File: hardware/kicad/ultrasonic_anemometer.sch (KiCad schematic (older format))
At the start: 0 parts

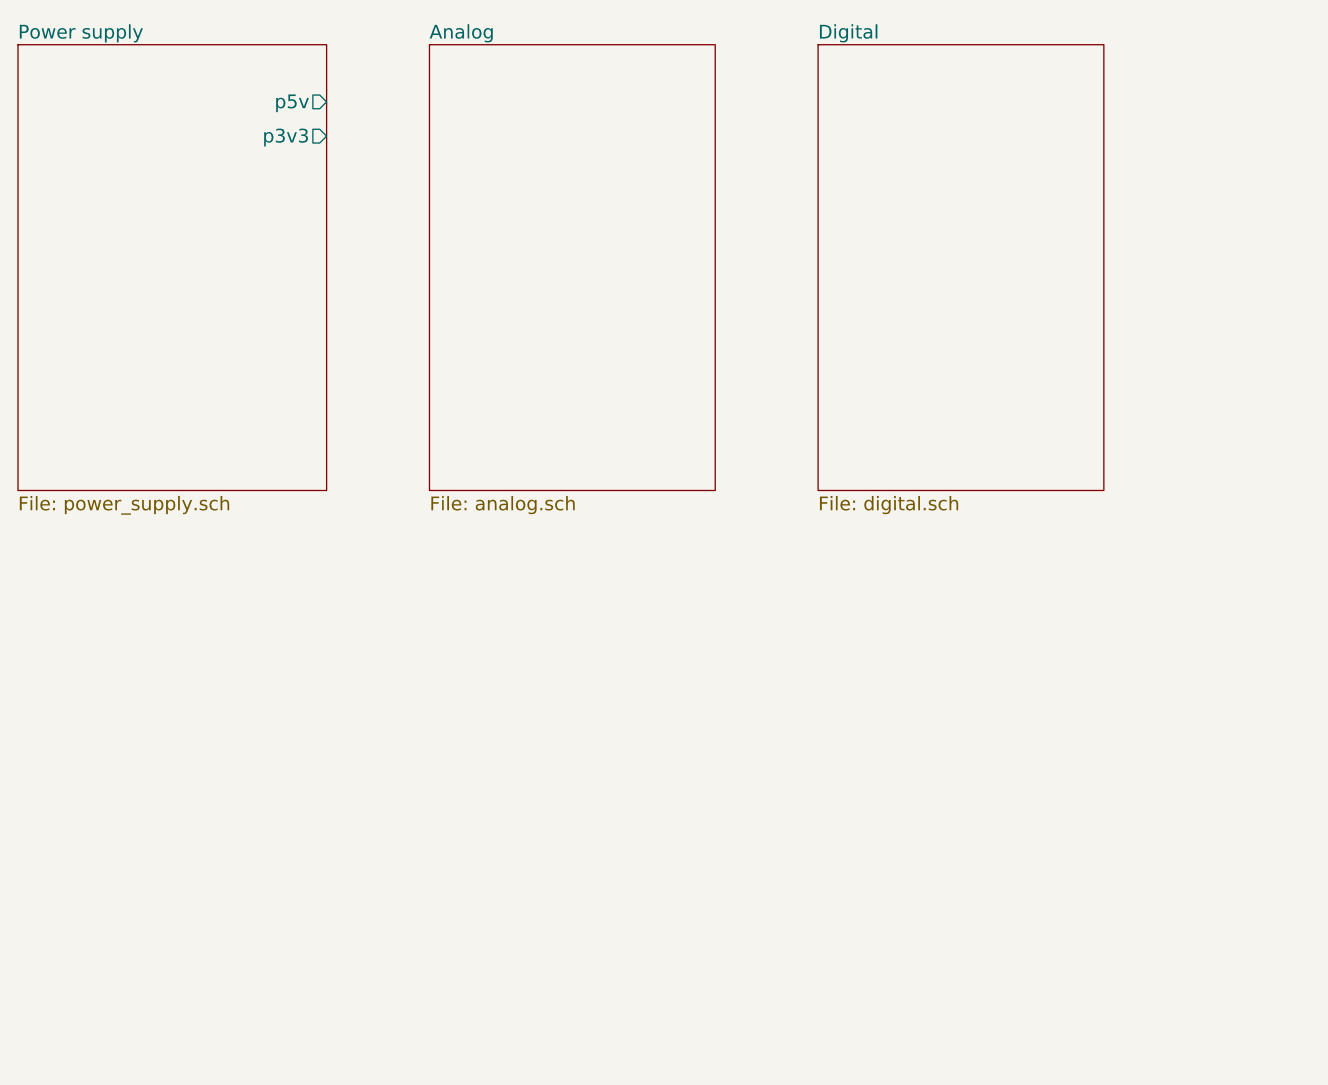
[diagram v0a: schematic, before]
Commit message: Added Modex library and hierarchial sheets for power, analog and digital circuitry.
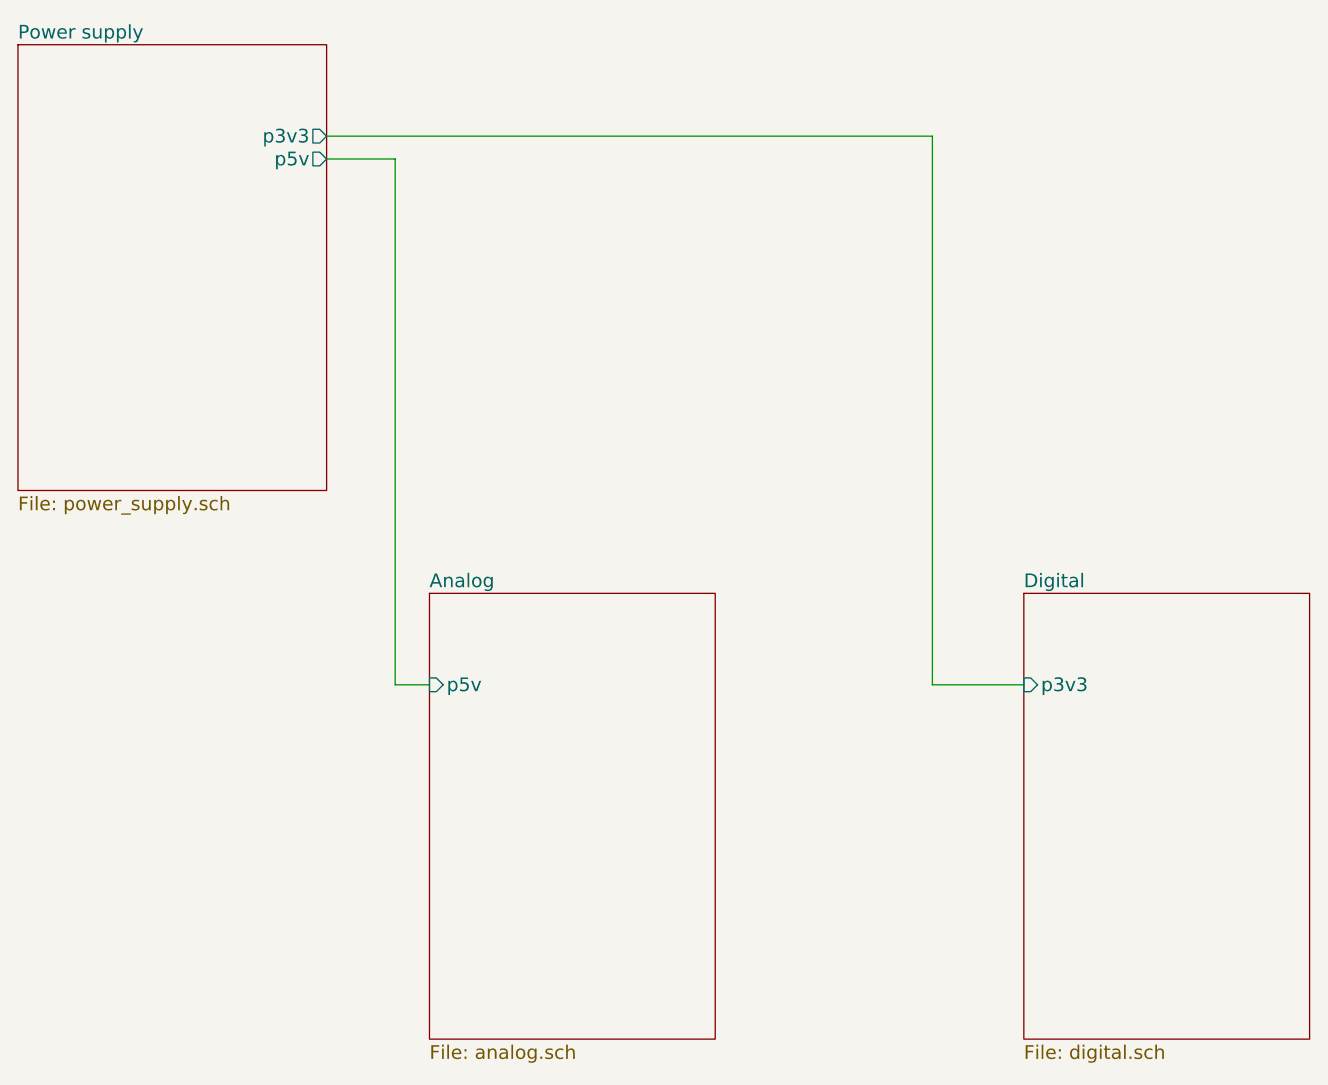
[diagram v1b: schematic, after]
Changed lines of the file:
@@
 LIBS:valves
 LIBS:microchip_dspic33dsc
+LIBS:modex
 LIBS:ultrasonic_anemometer-cache
 EELAYER 25 0
@@
 F0 "Power supply" 60
 F1 "power_supply.sch" 60
-F2 "p5v" O R 3750 1450 60
+F2 "p5v" O R 3750 1700 60
 F3 "p3v3" O R 3750 1600 60
 $EndSheet
 $Sheet
-S 4200 1200 1250 1950
+S 4200 3600 1250 1950
 U 57FA5DCE
 F0 "Analog" 60
 F1 "analog.sch" 60
+F2 "p5v" I L 4200 4000 60
 $EndSheet
 $Sheet
-S 5900 1200 1250 1950
+S 6800 3600 1250 1950
 U 57FA5DF6
 F0 "Digital" 60
 F1 "digital.sch" 60
+F2 "p3v3" I L 6800 4000 60
 $EndSheet
+Wire Wire Line
+	3750 1600 6400 1600
+Wire Wire Line
+	6400 1600 6400 4000
+Wire Wire Line
+	6400 4000 6800 4000
+Wire Wire Line
+	3750 1700 4050 1700
+Wire Wire Line
+	4050 1700 4050 4000
+Wire Wire Line
+	4050 4000 4200 4000
 $EndSCHEMATC

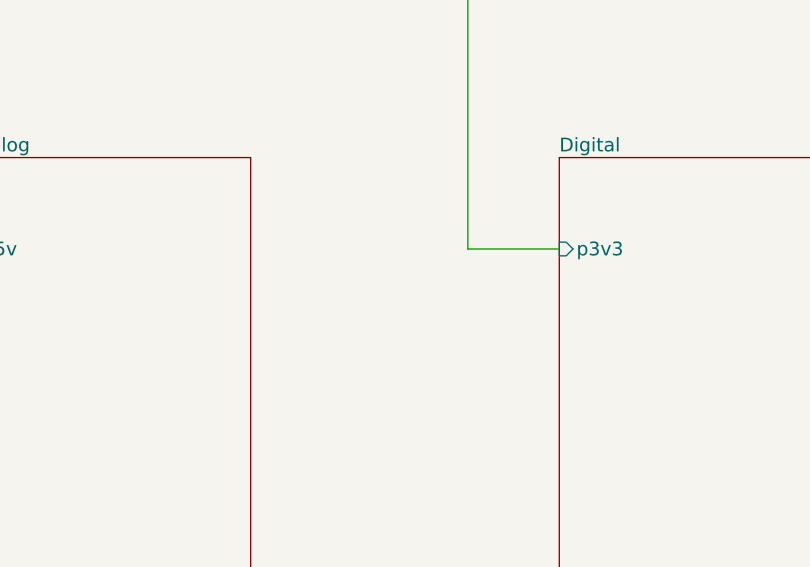
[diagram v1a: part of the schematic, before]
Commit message: Updated schematic and PCB.
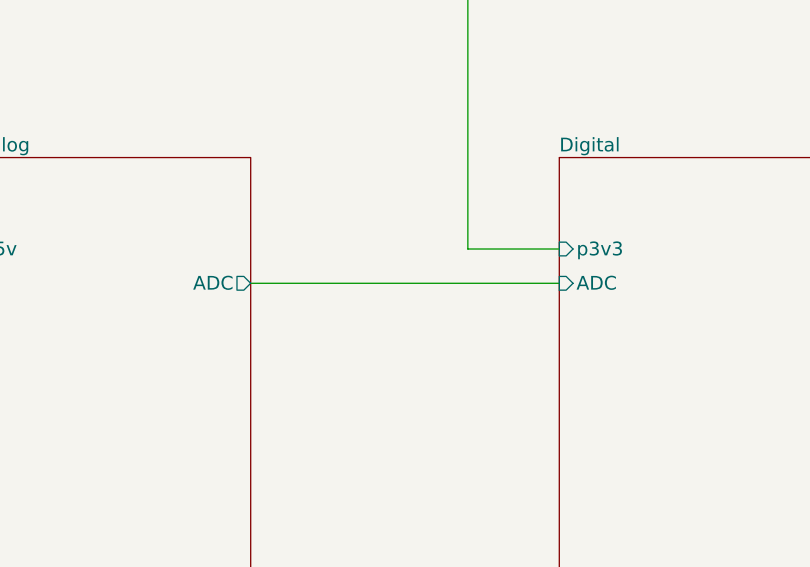
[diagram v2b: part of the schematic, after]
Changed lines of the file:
@@
 F1 "analog.sch" 60
 F2 "p5v" I L 4200 4000 60
+F3 "ADC" O R 5450 4150 60
 $EndSheet
 $Sheet
@@
 F1 "digital.sch" 60
 F2 "p3v3" I L 6800 4000 60
+F3 "ADC" I L 6800 4150 60
 $EndSheet
 Wire Wire Line
@@
 Wire Wire Line
 	4050 4000 4200 4000
+Wire Wire Line
+	5450 4150 6800 4150
 $EndSCHEMATC
